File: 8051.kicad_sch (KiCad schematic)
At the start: 37 parts, among them J1 Conn_01x02_Male, J2 Conn_02x30_Odd_Even, J3 Conn_01x02_Male, J4 Conn_01x02_Male, J5 Conn_01x01_Male, J6 Conn_01x04, SW1 SW_Push, U1 P87C51RB, U2 74HC244, U3 74LS373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

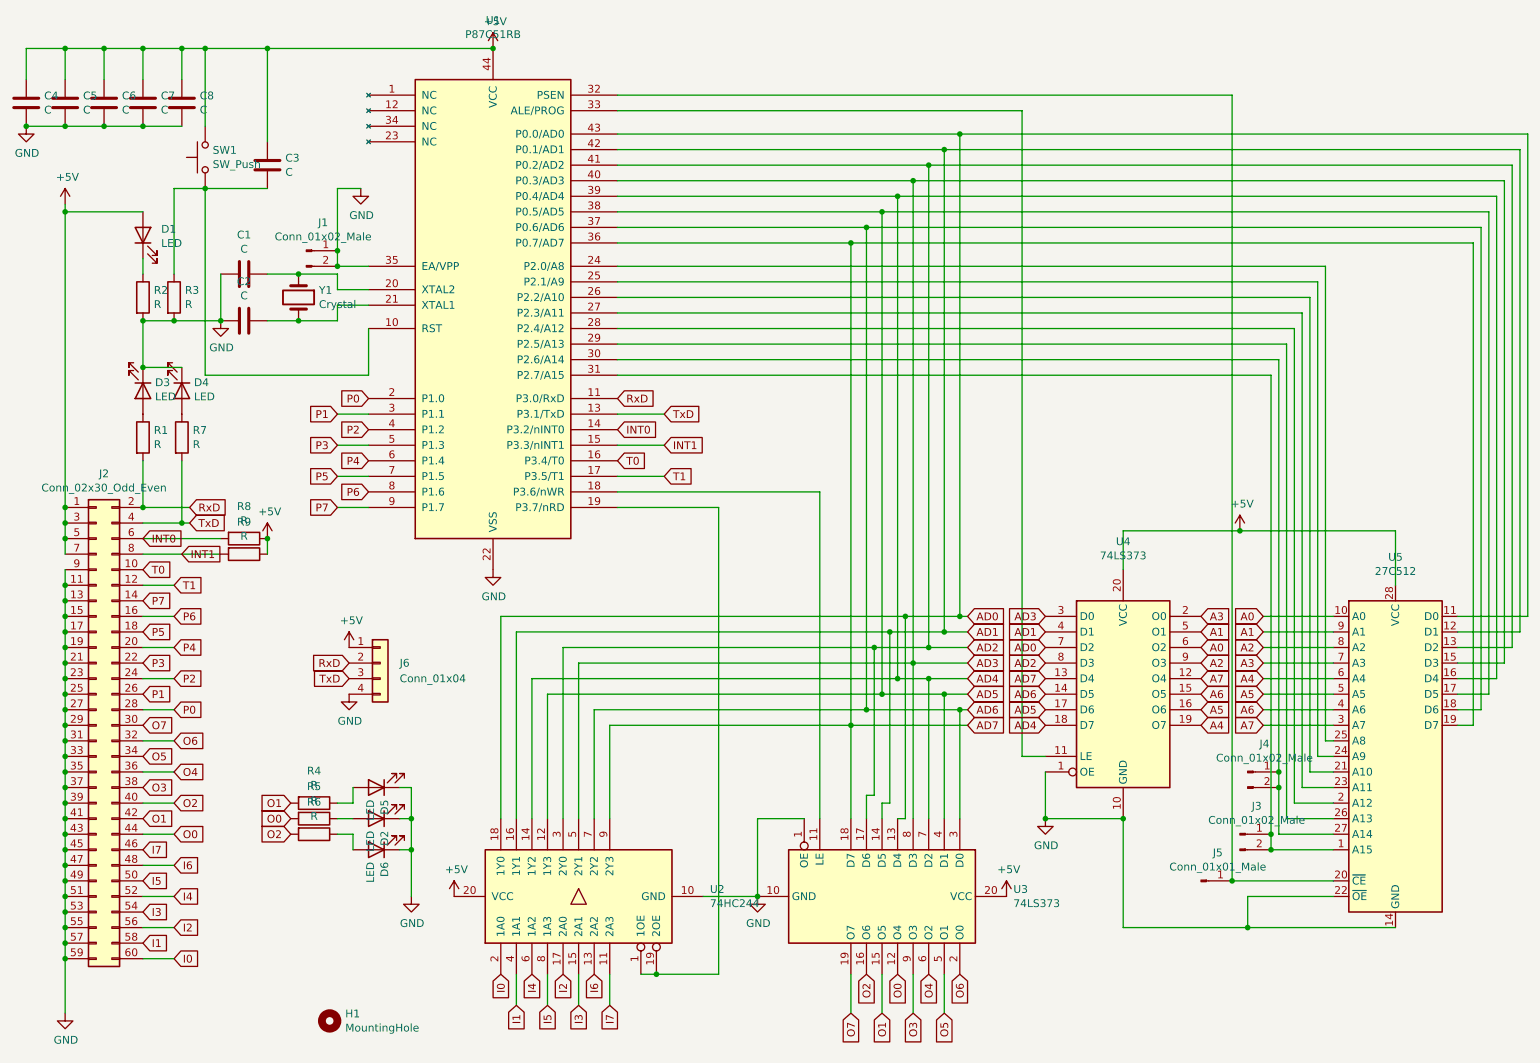
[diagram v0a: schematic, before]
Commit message: implement rue's errata; update to Kicad 8; revision 2
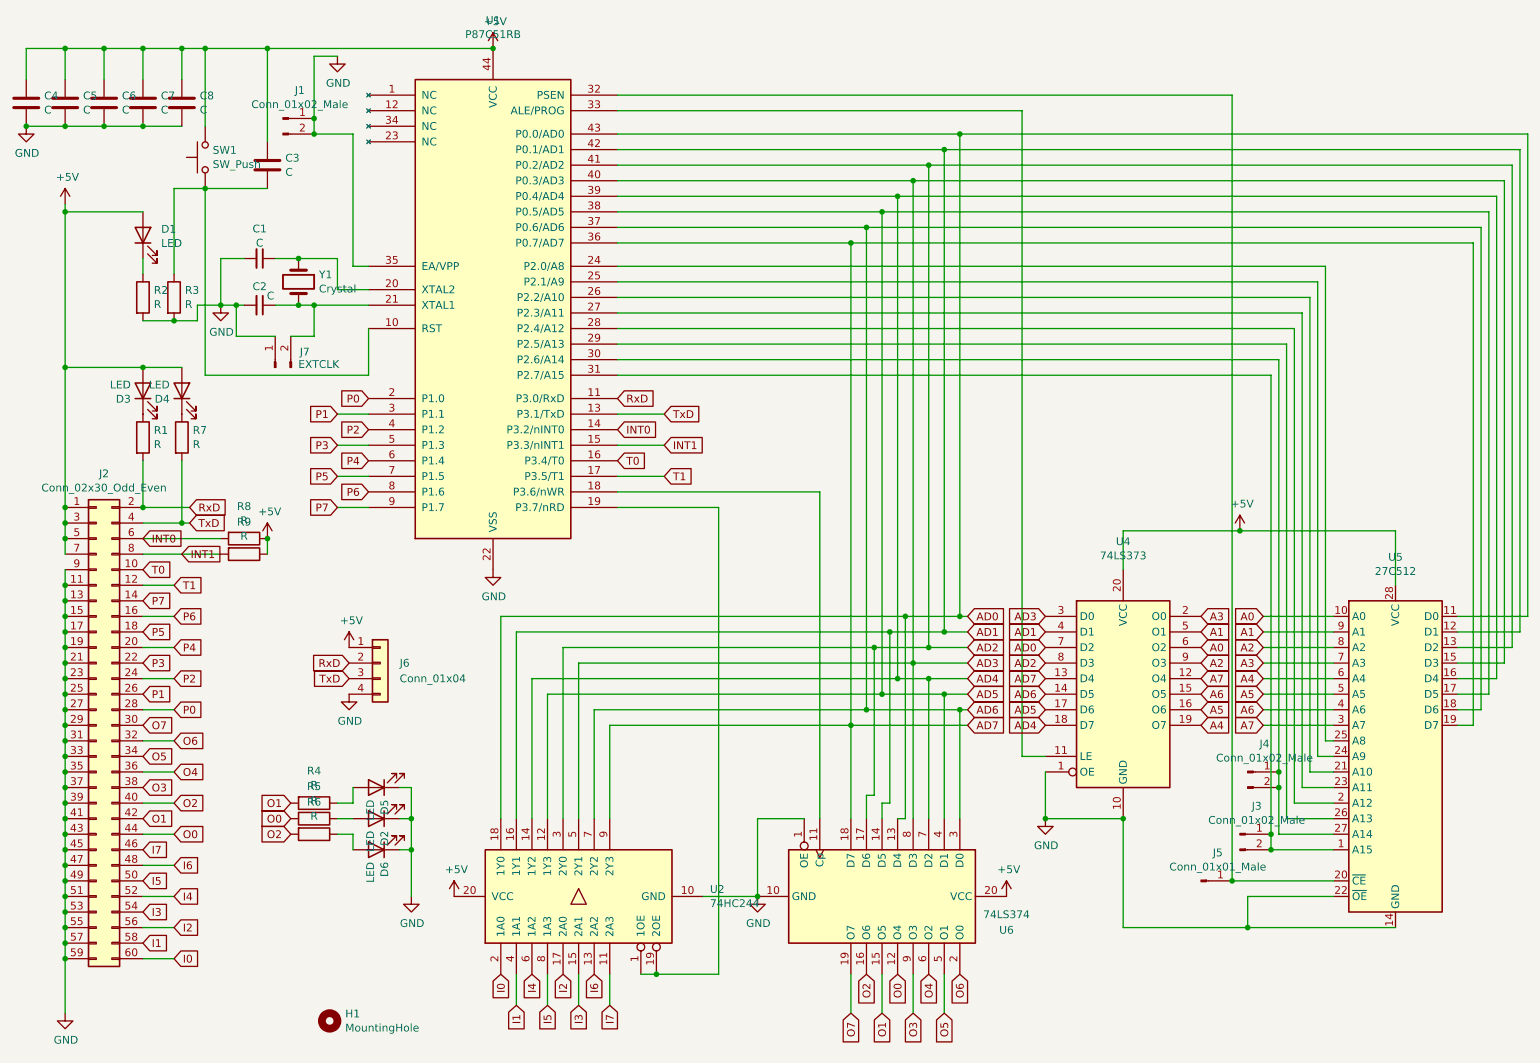
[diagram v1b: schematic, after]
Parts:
- removed U3: 74LS373, Package_SO:SOIC-20W_7.5x12.8mm_P1.27mm, symbol 74xx:74LS373
- added J7: EXTCLK, Connector_PinSocket_2.54mm:PinSocket_1x02_P2.54mm_Vertical, symbol 8051-rescue:Conn_01x02_Male-Connector
- added U6: 74LS374, Package_SO:SOIC-20W_7.5x12.8mm_P1.27mm, symbol 74xx:74LS374
- C1, C2: symbol Device:C -> Device:C_Small
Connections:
- net +5V: now also D3.2 (A), D4.2 (A), U6.20 (VCC)
- net AD0: now also U6.13 (D4)
- net AD1: now also U6.14 (D5)
- net AD2: now also U6.17 (D6)
- net AD3: now also U6.8 (D3)
- net AD4: now also U6.7 (D2)
- net AD5: now also U6.4 (D1)
- net AD6: now also U6.3 (D0)
- net AD7: now also U6.18 (D7)
- net GND: now also J7.1 (Pin_1), U6.1 (OE), U6.10 (GND); no longer D3.1 (K), D4.1 (K)
- net O0: now also U6.12 (O4)
- net O1: now also U6.15 (O5)
- net O2: now also U6.16 (O6)
- net O3: now also U6.9 (O3)
- net O4: now also U6.6 (O2)
- net O5: now also U6.5 (O1)
- net O6: now also U6.2 (O0)
- net O7: now also U6.19 (O7)
- net at U1.18 (P3.6/nWR): now also U6.11 (Cp)
- net at C2.1, U1.21 (XTAL1), Y1.2: now also J7.2 (Pin_2)
- net at R1.1: now also D3.1 (K); no longer D3.2 (A)
- net at R7.1: now also D4.1 (K); no longer D4.2 (A)
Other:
- moved on the sheet: C1, C2, D3, D4, J1, Y1
